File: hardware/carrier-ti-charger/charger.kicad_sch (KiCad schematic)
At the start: 42 parts, among them J2 NTC, Q10 2N7002, Q12 2N7002, Q13 CSD17575Q3, SW4 RESET 6x6, U14 TPS259474LRPWR, U4 BQ25798RQMR

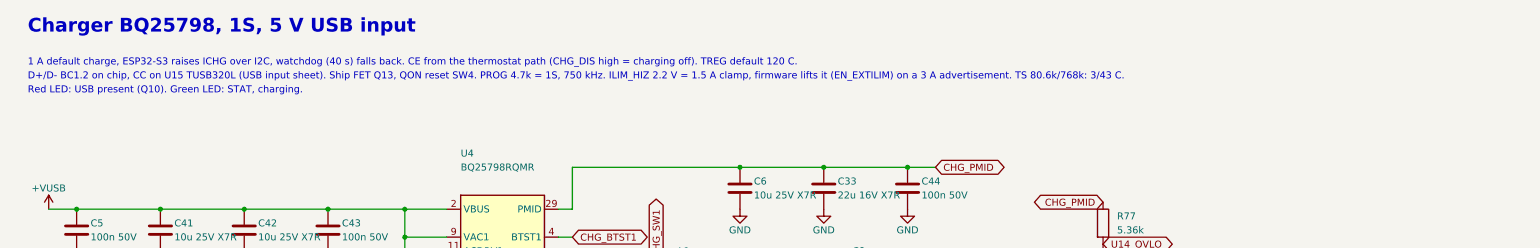
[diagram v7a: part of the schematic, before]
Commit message: Switch to faster FUSB303B USB controller.
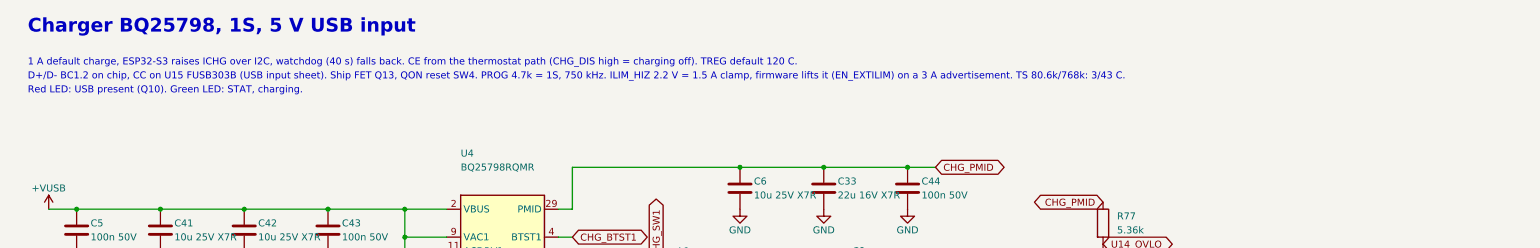
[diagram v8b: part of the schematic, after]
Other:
- note added: "D+/D- BC1.2 on chip, CC on U15 FUSB303B (USB input sheet). Ship FET Q13, QON reset SW4. PROG 4.7k = 1S, 750 kHz. ILIM_HIZ 2.2 V = 1.5 A clamp, firmware lifts it (EN_EXTILIM) on a 3 A advertisement. TS 80.6k/768k: 3/43 C."
- note removed: "D+/D- BC1.2 on chip, CC on U15 TUSB320L (USB input sheet). Ship FET Q13, QON reset SW4. PROG 4.7k = 1S, 750 kHz. ILIM_HIZ 2.2 V = 1.5 A clamp, firmware lifts it (EN_EXTILIM) on a 3 A advertisement. TS 80.6k/768k: 3/43 C."
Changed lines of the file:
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@@
 		)
 	)
-	(text "D+/D- BC1.2 on chip, CC on U15 TUSB320L (USB input sheet). Ship FET Q13, QON reset SW4. PROG 4.7k = 1S, 750 kHz. ILIM_HIZ 2.2 V = 1.5 A clamp, firmware lifts it (EN_EXTILIM) on a 3 A advertisement. TS 80.6k/768k: 3/43 C."
+	(text "D+/D- BC1.2 on chip, CC on U15 FUSB303B (USB input sheet). Ship FET Q13, QON reset SW4. PROG 4.7k = 1S, 750 kHz. ILIM_HIZ 2.2 V = 1.5 A clamp, firmware lifts it (EN_EXTILIM) on a 3 A advertisement. TS 80.6k/768k: 3/43 C."
 		(exclude_from_sim no)
 		(at 20.32 30.48 0)
